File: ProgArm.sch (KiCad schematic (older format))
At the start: 118 parts, among them M1 MOTOR, P1 I2C_Port, P3 SPI_Port, P9 MicroUSB, Q1 MOS_P, Q10 MOS_P, Q11 MOS_P, Q5 MOS_P, Q7 MOS_P, Q8 MOS_P, Q9 MOS_P, SW1 ON/OFF, U1 STM32F103R, X1 32.768(MS3V-T1R), X2 8MHz

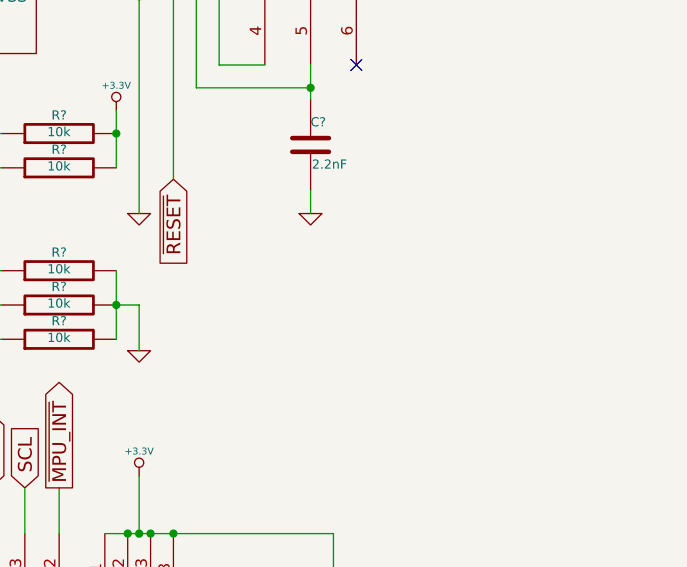
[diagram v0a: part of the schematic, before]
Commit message: Issue with bluetooth pull-downs
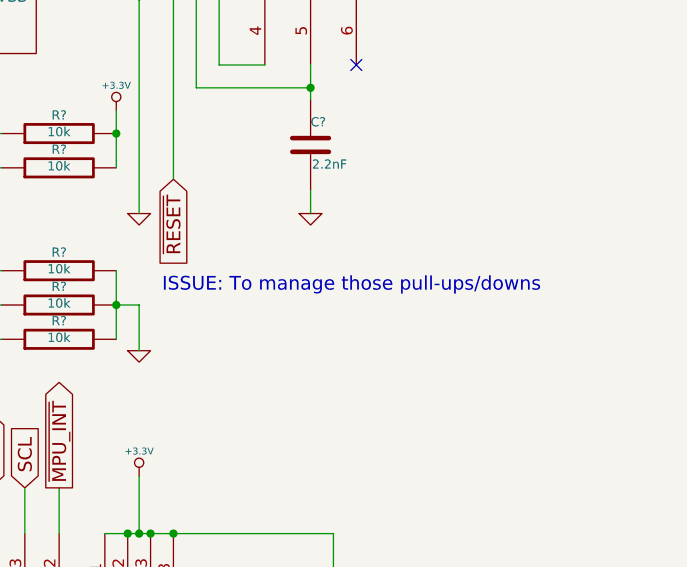
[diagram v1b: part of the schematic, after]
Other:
- note added: "ISSUE: To manage those pull-ups/downs"
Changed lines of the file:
@@
 	5800 5900 5950 5900
 Connection ~ 5850 5750
+Text Notes 14100 7050 0    60   ~ 0
+ISSUE: To manage those pull-ups/downs
 $EndSCHEMATC

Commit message: Cleaning. (halfway through)
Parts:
- removed P1: I2C_Port, symbol CONN_6
- added P?: I²C Port, symbol CONN_4
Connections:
- net labels removed: I2C_EXTRA1, I2C_EXTRA2
- wire segments 448 -> 501
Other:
- note added: "TODO pullups"
- moved on the sheet: Q10, R27, R30

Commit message: Rearranging pins
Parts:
- removed RING_PORT: CONN_9, symbol CONN_9
- added K?: RING_LEDS, symbol CONN_3
- added P?: RING_IR_OUT, symbol CONN_1
- added P?: RING_BUTTONS, symbol CONN_2
- added P?: RING_VCC, symbol CONN_1
- added P?: RING_GND, symbol CONN_1
- added RING_GPIO_1: CONN_1, symbol CONN_1
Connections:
- net labels added: BT_RXD, BT_TXD, LED_B_OUT, LED_G_OUT, LED_IR_OUT, LED_R_OUT, RING_BTN1_OUT, RING_GPIO_1
- net labels removed: IR_SIGNAL
- wire segments 501 -> 414
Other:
- moved on the sheet: Q10, Q7, Q8, Q9, Q?, R18, R19, R20, R22, R23, R24, R27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

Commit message: Rearranged pins, extra ports, etc.
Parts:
- added P?: UART_Port, symbol CONN_4
- added P?: TIM1_Port, symbol CONN_1
- added P?: GPIOA_Port_1_2, symbol CONN_2
- added P?: GPIOA_Port_1, symbol CONN_1
- P?: renamed from T_SENS; value CONN_1 -> T_SENS
- P?: renamed from RXD; value CONN_1 -> RXD
- P?: renamed from TXD; value CONN_1 -> TXD
- P?: value I²C Port -> I²C_Port
- P?: renamed from RING_GPIO_1; value CONN_1 -> RING_GPIO_1
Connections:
- net GND: now also P?.4 (P4), P?.4 (P4); no longer P?.1 (P1)
- net I2C_SCL: now also P?.3 (P3); no longer P?.2 (P2)
- net I2C_SDA: now also P?.2 (P2); no longer P?.3 (P3)
- net IN_CURRENT: now also U1.8 (ADC1_IN10/PC0)
- net PORT_POWER: now also P?.1 (P1), P?.1 (P1); no longer P?.4 (P4)
- net RING_GPIO_1: now also U1.20 (SPI1_NSS/ADC1_IN4/USART2_CK/DAC1_OUT/PA4)
- net ~GAUGE_INT: now also U1.39 (PC8)
- net ~LPS_INT: now also U1.52 (PC11)
- net ~MPU_INT: now also U1.51 (PC10)
- net ~OTG_cable: now also U1.25 (ADC1_IN15/PC5)
- net ~PMIC_INT: now also U1.40 (PC9)
- net ~PORT_PWR_ENABLE: now also U1.27 (PB1/ADC1_IN9/TIM3_CH4)
- net ~RDYN: now also U1.38 (PC7)
- net ~REQN: now also U1.37 (PC6)
- net ~RING_BTN2: now also U1.9 (ADC1_IN11/PC1)
- net ~SI_INT: now also U1.53 (PC12)
- net ~VIBRATION: now also U1.61 (PB8/TIM4_CH3/TIM16_CH1/CEC)
- net GPIOA_1: now reaches U1.10 (ADC1_IN12/PC2)
- net GPIOA_1: now also P?.1 (P1)
- net GPIOA_2: now reaches U1.11 (ADC1_IN13/PC3)
- net GPIOA_2: now also P?.2 (PM)
- net RING_GPIOA_1: now reaches U1.24 (ADC1_IN14/PC4)
- net RING_GPIOA_1: now also P?.1
- net LED_IR: now reaches U1.26 (PB0/ADC1_IN8/TIM3_CH3)
- net LED_IR: now also R?.2
- net TIM1: now reaches U1.41 (USART1_CK/MCO/TIM1_CH1/PA8)
- net TIM1: now also P?.1
- net USART_TX: now reaches U1.42 (USART1_TX/TIM1_CH2/TIM15_BKIN/PA9)
- net USART_TX: now also P?.2 (P2)
- net USART_RX: now reaches U1.43 (USART1_RX/TIM1_CH3/TIM17_BKIN/PA10)
- net USART_RX: now also P?.3 (P3)
- removed net ~LED_IR: R?.2, U1.20 (SPI1_NSS/ADC1_IN4/USART2_CK/DAC1_OUT/PA4)
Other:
- moved on the sheet: BT2, C?, D3, D?, JP1, L?, M1, P3, P?, Q11, R28, R34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

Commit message: Fixed issues from the list, added block-style grouping
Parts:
- removed R2, R3: 4k7, ~, symbol R
- added C?: 100nF, ~, symbol C
- added R? (x2): 10k, ~, symbol R
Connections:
- net GND: now also C?.2
- net SCL: now also R?.1
- net SDA: now also R?.1
- net VCC: now also C?.1
- net at C?.1, U?.2 (REG25), U?.5 (VCC): now also R?.2, R?.2
- no-connect marks 10 -> 7
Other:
- note added: "Bluetooth RF System"
- note added: "General Purpose IO Ports\nand Data Transfer Interfaces"
- note added: "Human Interface Devices"
- note added: "IIC Sensors"
- note added: "Main Controller And RTC Backup System"
- note added: "Power Management System"
- note added: "USB Interface and Charging Port"
- note removed: "ISSUE: To manage those pull-ups/downs"
- note removed: "TODO pullups"
- moved on the sheet: A?, B?, BT2, C23, C24, C?, D3, D?, JP1, L3, L?, M1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

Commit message: Managed capacitors, made some cosmetic improvements
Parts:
- removed C3: 100nF, ~, symbol C
- added C? (x2): 100nF, ~, symbol C
- C11, C15: value 20pF -> 18pF
- C12, C8: value 12pF -> 6pF
- C?: value 0.1F -> 0.03F
- L1: value 1uH -> 2.2uH
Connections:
- net +3.3V: now also C?.1
- net GND: now also C?.1, C?.2
- net at R?.2, U1.1 (VBAT), U?.5 (OUT): now also C?.2
- net LED_IR renamed ~LED_IR
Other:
- moved on the sheet: BT2, C1, C?, JP1, P?, R?, U?

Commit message: Pulse meter LEDs are now powered from VCC
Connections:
- net +3.3V: no longer R?.1
- net VCC: now also R?.1
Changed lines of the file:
@@
 	8550 5450 8550 5750
-Wire Wire Line
-	8550 4950 11500 4950
 Wire Wire Line
 	8550 4950 8550 5050
@@
 Wire Wire Line
 	10950 5500 10950 4950
-Connection ~ 10950 4950
 Wire Wire Line
 	12400 2250 12400 2200
@@
 Connection ~ 10800 6550
 Connection ~ 8850 6300
+Wire Wire Line
+	10950 4950 8550 4950
+$Comp
+L VCC #PWR?
+U 1 1 5485184B
+P 11450 4900
+F 0 "#PWR?" H 11450 5000 30  0001 C CNN
+F 1 "VCC" H 11450 5000 30  0000 C CNN
+F 2 "" H 11450 4900 60  0000 C CNN
+F 3 "" H 11450 4900 60  0000 C CNN
+	1    11450 4900
+	1    0    0    -1
+$EndComp
+Wire Wire Line
+	11450 4900 11450 4950
+Wire Wire Line
+	11450 4950 11500 4950
 $EndSCHEMATC

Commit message: Automatic component annotation
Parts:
- gave numbers to parts that had none: 81
- renumbered BT2 to BT1, C12 to C10, C15 to C12, C4 to C18, C23 to C33, C24 to C36, C5 to C4, C8 to C6, D3 to D4, L1 to L2, L3 to L5, P9 to P16, P3 to P2, Q5 to Q2, Q7 to Q3, Q8 to Q4, Q9 to Q5, Q10 to Q7, Q11 to Q8, R6 to R1, R15 to R12, R17 to R13, R18 to R17, R19 to R18, R20 to R19, R22 to R21, R23 to R22, R24 to R23, R30 to R29, R4 to R3, R34 to R30, R31 to R38, R32 to R39, R33 to R4, R1 to R7, U1 to U4
